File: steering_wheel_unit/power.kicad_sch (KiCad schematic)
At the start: 23 parts, among them IC2 LM76202QPWPRQ1, U6 TPS62933

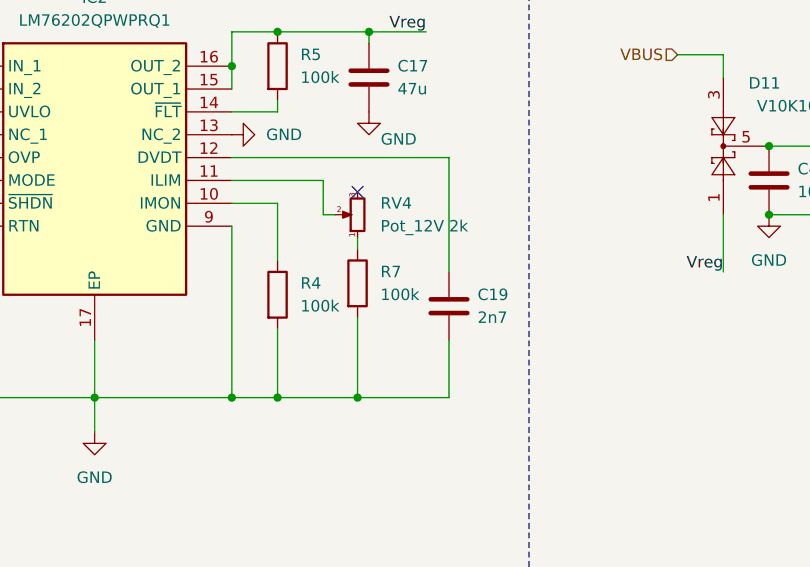
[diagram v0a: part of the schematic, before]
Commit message: change usb c connector
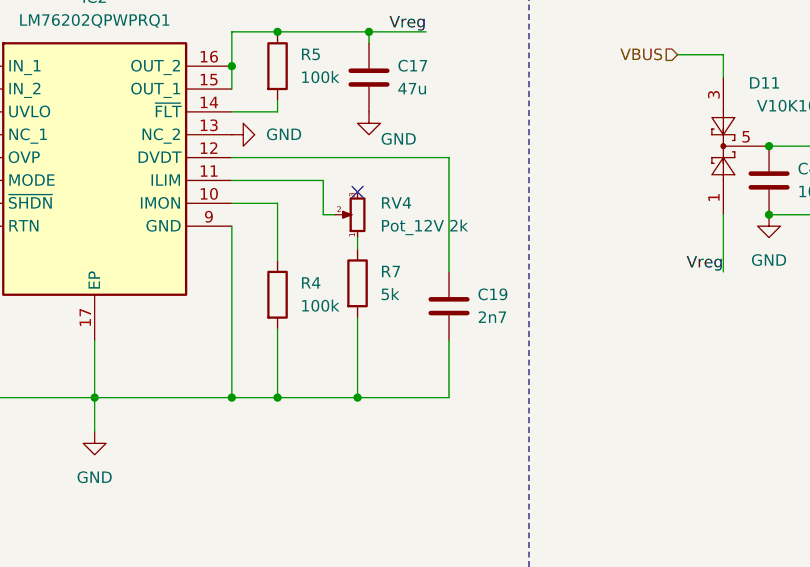
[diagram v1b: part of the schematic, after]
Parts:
- R7: value 100k -> 5k
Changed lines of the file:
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@@
 		(fields_autoplaced yes)
 		(property "Reference" "R7"
-			(at 123.19 58.42 0)
+			(at 123.19 58.4199 0)
 			(effects
 				(font
@@
 			)
 		)
-		(property "Value" "100k"
-			(at 123.19 60.96 0)
+		(property "Value" "5k"
+			(at 123.19 60.9599 0)
 			(effects
 				(font
